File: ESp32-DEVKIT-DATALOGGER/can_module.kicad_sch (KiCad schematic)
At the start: 11 parts, among them J401 RJ45, J402 Conn_01x02_Socket, U401 ISO1050DUB, U402 TJA1051T

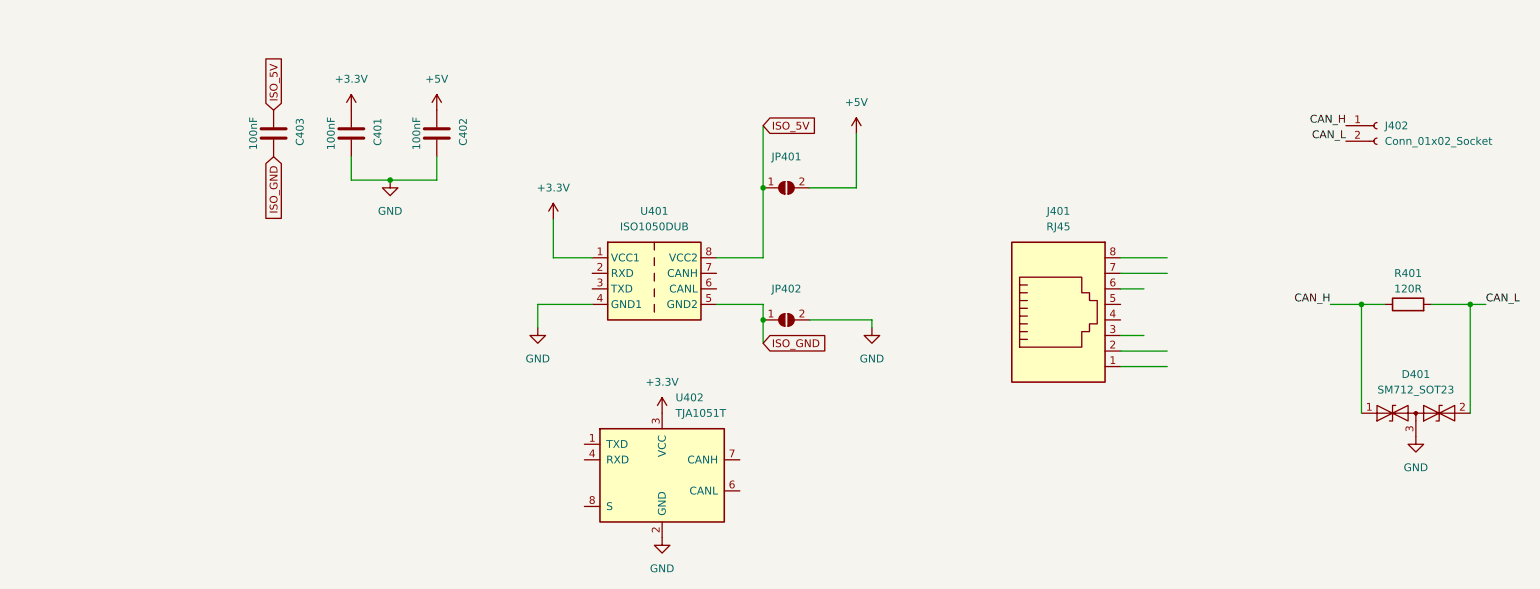
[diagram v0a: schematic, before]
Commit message: Small Changes
Adding I2C components
More RS485
And it is required changing the  Labels for RS485 . for 3 different channels
And Make them ISO Pins
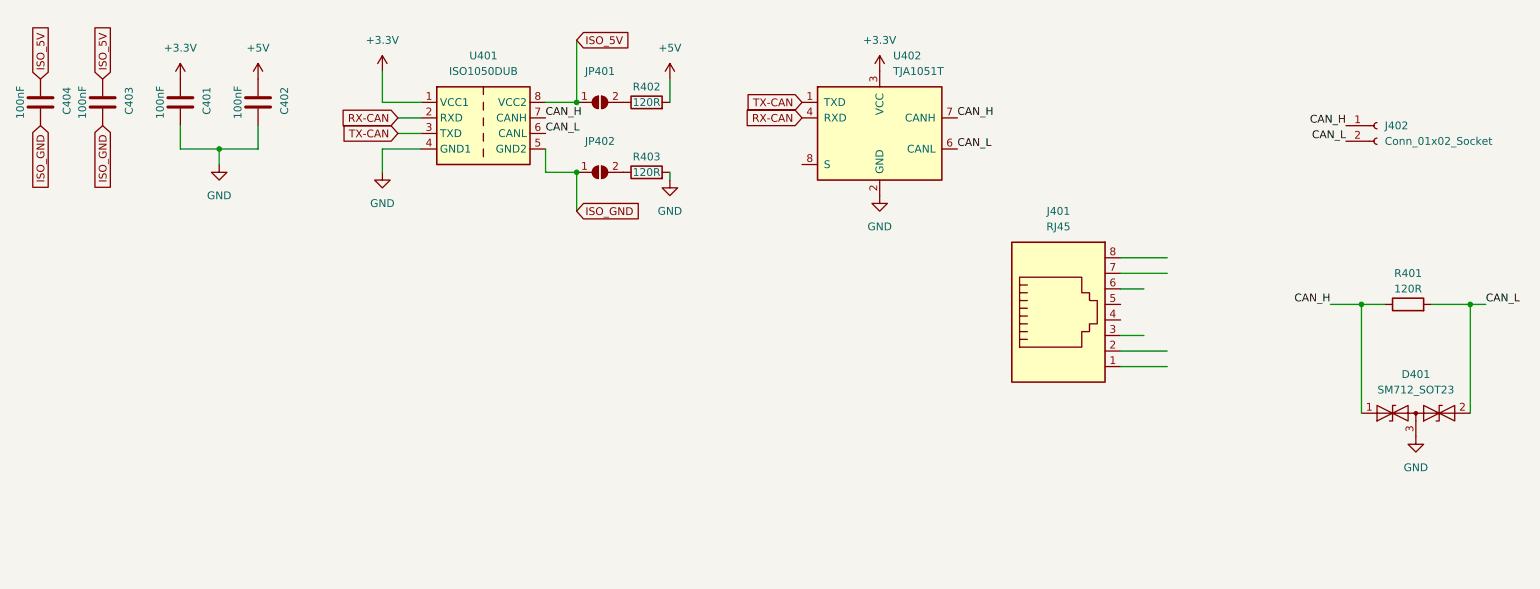
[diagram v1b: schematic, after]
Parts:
- added C404: 100nF, Capacitor_SMD:C_0603_1608Metric_Pad1.08x0.95mm_HandSolder, symbol Device:C
- added R402, R403: 120R, Resistor_SMD:R_2512_6332Metric_Pad1.40x3.35mm_HandSolder, symbol Device:R
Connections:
- net +5V: now also R402.2; no longer JP401.2 (B)
- net CAN_H: now also U401.7 (CANH), U402.7 (CANH)
- net CAN_L: now also U401.6 (CANL), U402.6 (CANL)
- net GND: now also R403.2; no longer JP402.2 (B)
- net ISO_5V: now also C404.2
- net ISO_GND: now also C404.1
- net RX-CAN: now reaches U401.2 (RXD)
- net RX-CAN: now also U402.4 (RXD)
- net TX-CAN: now reaches U401.3 (TXD)
- net TX-CAN: now also U402.1 (TXD)
- new net: JP401.2 (B), R402.1
- new net: JP402.2 (B), R403.1
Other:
- moved on the sheet: C401, C402, C403, JP401, JP402, U401, U402
